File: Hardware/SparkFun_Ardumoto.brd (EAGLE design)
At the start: 59.7 x 53.3 mm, 64 parts, among them U1 ARDUINO, U2 L298, U5 74HC1G04, U6 74HC1G04

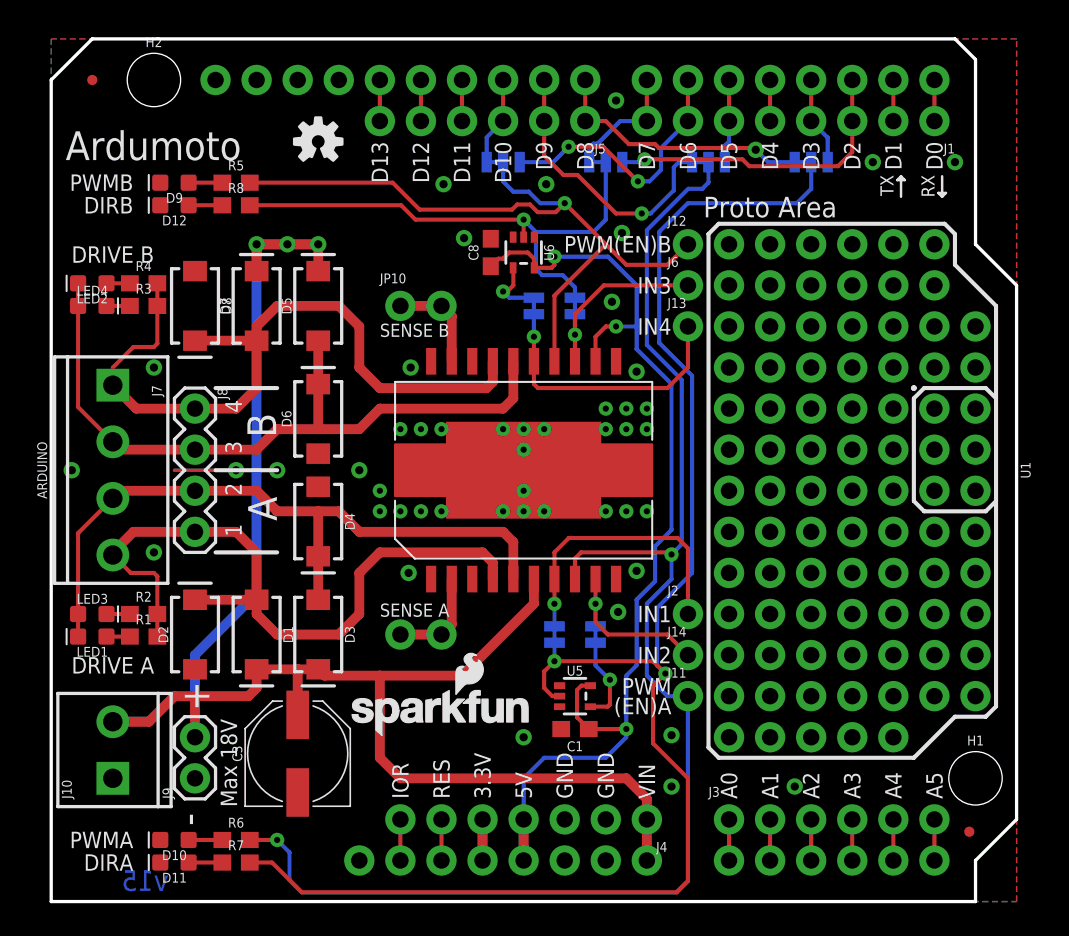
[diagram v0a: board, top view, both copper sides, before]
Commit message: Made changes to prototype in preparation for reds
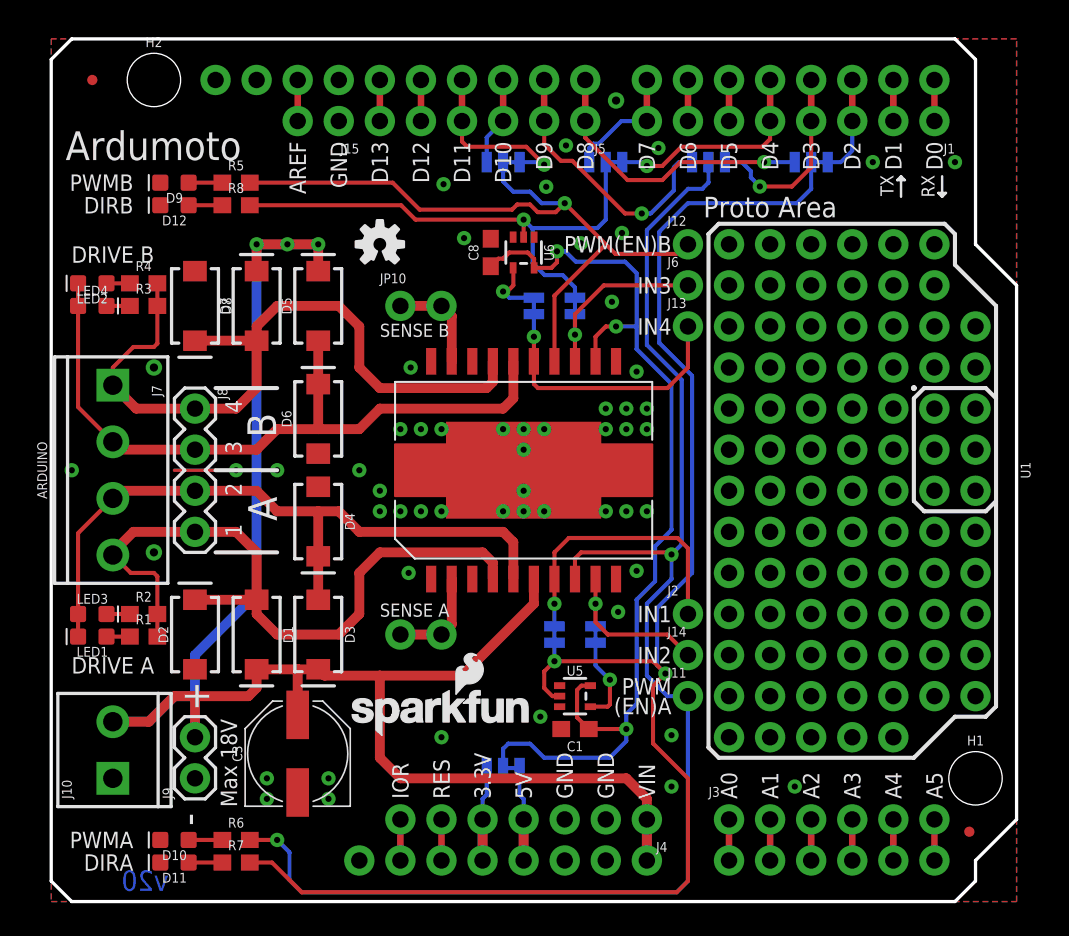
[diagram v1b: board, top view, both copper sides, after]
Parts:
- added J15: (no value), SparkFun-Connectors:1X02_NO_SILK
- added JP11: 31NCT, SparkFun-Jumpers:SMT-JUMPER_3_1-NC_TRACE_SILK
- moved U$1 7.41 mm to (20.3, 40.6)
- turned JP1 to 180 degrees
- turned JP2 to 180 degrees
- turned JP3 to 180 degrees
- turned JP4 to 180 degrees
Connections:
- new net N$10: J15.2, U1.AREF
- new net VCCIO: C1.1, C8.1, JP11.2, U2.12, U5.5, U6.5
- net 3.3V: now also JP11.1
- net 5V: now also JP11.3; no longer C1.1, C8.1, U2.12, U5.5, U6.5
- net D10: now also JP4.1; no longer JP4.3
- net D11: now also JP4.3
- net D2: now also JP1.3; no longer JP3.1
- net D3: now also JP2.3; no longer JP1.1
- net D4: now also JP3.3
- net D5: no longer JP2.1
- net D6: no longer JP4.1
- net D7: now also JP3.1; no longer JP3.3
- net D8: now also JP1.1; no longer JP1.3
- net D9: now also JP2.1; no longer JP2.3
- net GND: now also J15.1
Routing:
- net VCCIO: track 0.00 -> 62.5 mm, vias 0 -> 3
- net 5V: track 66.7 -> 8.36 mm, vias 3 -> 0
- net D6: track 16.6 -> 2.54 mm, vias 2 -> 0
- net D2: track 19.3 -> 6.19 mm, vias 1 -> 0
- net D4: track 2.54 -> 14.6 mm, vias 0 -> 1
- net D11: track 2.54 -> 11.1 mm, vias 0 -> 1
- net D3: track 5.50 -> 12.1 mm, vias 0 -> 1
- net 3.3V: track 5.08 -> 8.36 mm
- net D5: track 5.19 -> 2.54 mm
- net N$10: track 0.00 -> 2.54 mm
- net D8: track 16.5 -> 18.1 mm
- net PWMB: track 44.6 -> 44.0 mm
- net GND: vias 48 -> 56
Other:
- outline, holes or cut-outs redrawn
- board text added: "AREF"
- board text added: "VCCIO"
- board text added: "v20"
- board text removed: "5"
- board text removed: "6"
- board text removed: "v15"

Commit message: Added note on VCCIO and nudged traces
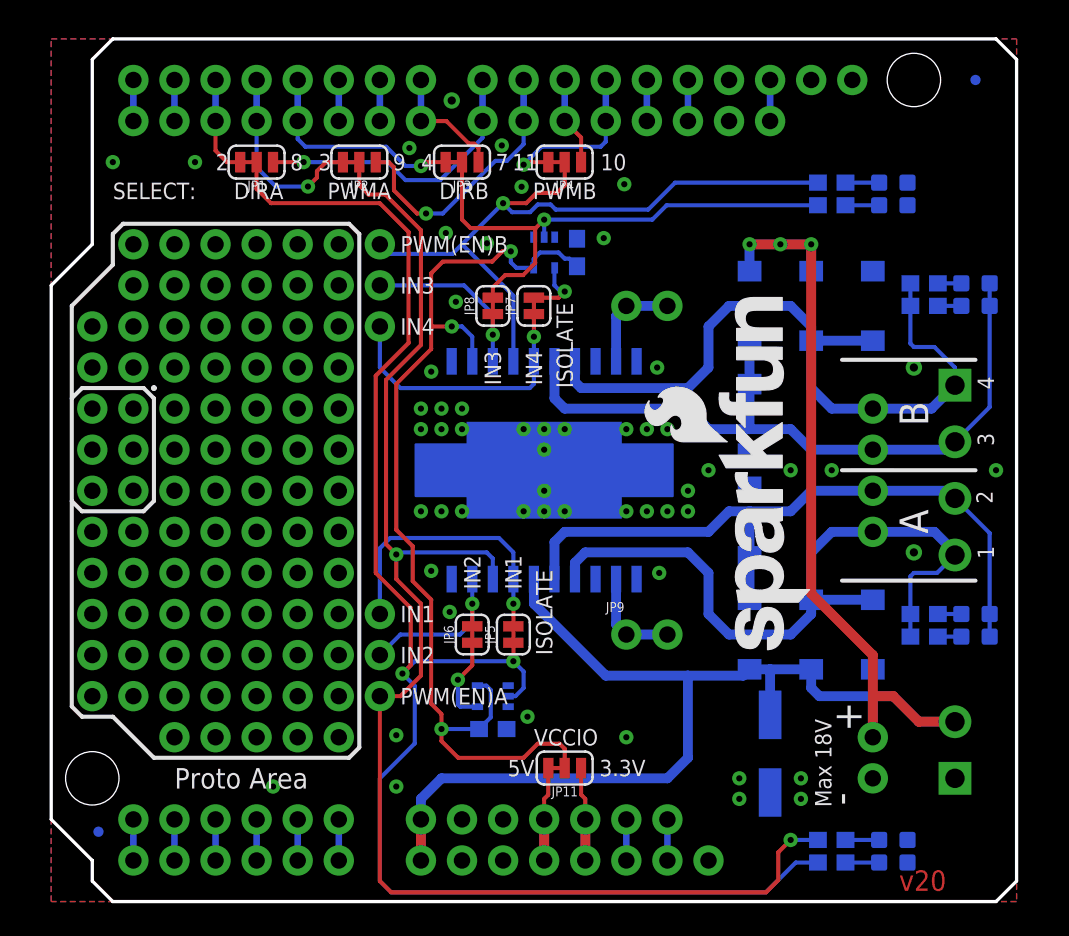
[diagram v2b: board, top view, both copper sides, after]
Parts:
- moved FRAME2 105.4 mm to (82.5, -11.4), flipped to the bottom
- moved FRAME1 64.8 mm to (62.3, -15.2), flipped to the bottom
- moved FD1 54.6 mm to (57.1, 50.8), flipped to the bottom
- moved H1 54.6 mm to (2.54, 7.62), flipped to the bottom
- moved LED1 54.6 mm to (57.1, 16.4), flipped to the bottom
- moved LED2 54.6 mm to (57.1, 38.2), flipped to the bottom
- moved LED3 54.6 mm to (57.1, 17.8), flipped to the bottom
- moved LED4 54.6 mm to (57.1, 36.8), flipped to the bottom
- moved FD2 53.8 mm to (2.92, 4.32), flipped to the bottom
- moved J10 52.1 mm to (55.9, 7.62), flipped to the bottom
- moved J7 52.1 mm to (55.9, 31.9), flipped to the bottom
- moved J1 49.5 mm to (5.08, 48.3), flipped to the bottom
- moved R1 48.3 mm to (54.0, 16.4), flipped to the bottom
- moved R2 48.3 mm to (54.0, 17.8), flipped to the bottom
- moved R3 48.3 mm to (54.0, 36.8), flipped to the bottom
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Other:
- outline, holes or cut-outs redrawn

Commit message: Made post-review changes
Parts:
- moved FRAME2 105.4 mm to (-22.9, -11.4), flipped to the top
- moved FRAME1 64.8 mm to (-2.56, -15.2), flipped to the top
- moved FD1 54.6 mm to (2.54, 50.8), flipped to the top
- moved H1 54.6 mm to (57.1, 7.62), flipped to the top
- moved LED1 54.6 mm to (2.54, 16.4), flipped to the top
- moved LED2 54.6 mm to (2.54, 38.2), flipped to the top
- moved LED3 54.6 mm to (2.54, 17.8), flipped to the top
- moved LED4 54.6 mm to (2.54, 36.8), flipped to the top
- moved FD2 53.8 mm to (56.8, 4.32), flipped to the top
- moved J10 52.1 mm to (3.81, 7.62), flipped to the top
- moved J7 52.1 mm to (3.81, 31.9), flipped to the top
- moved J1 49.5 mm to (54.6, 48.3), flipped to the top
- moved R1 48.3 mm to (5.71, 16.4), flipped to the top
- moved R2 48.3 mm to (5.71, 17.8), flipped to the top
- moved R3 48.3 mm to (5.71, 36.8), flipped to the top
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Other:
- outline, holes or cut-outs redrawn

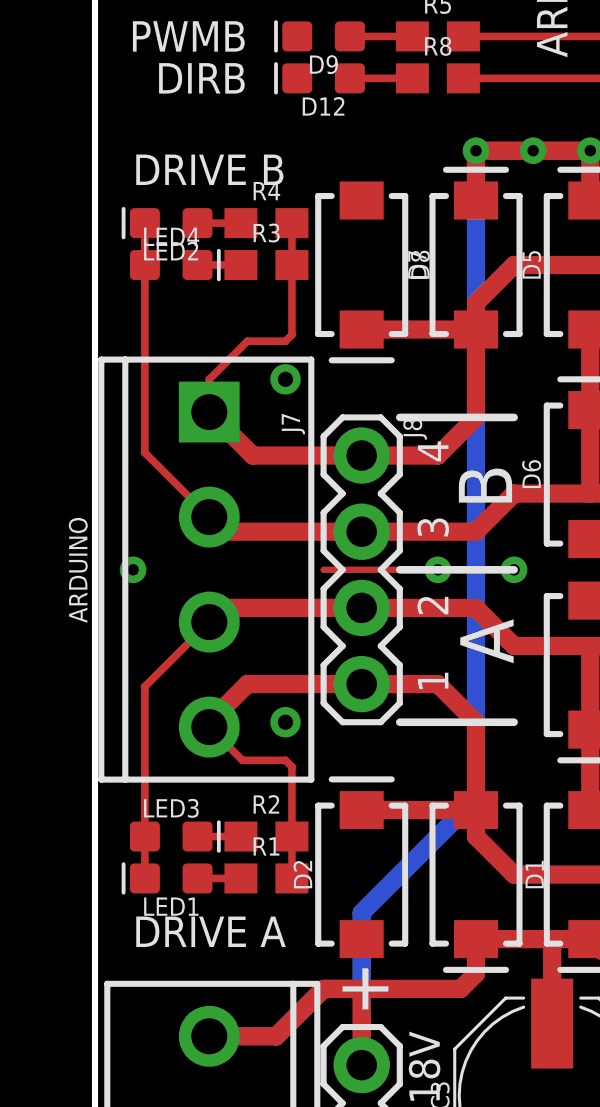
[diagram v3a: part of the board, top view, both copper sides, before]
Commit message: switched components LED1 and LED3
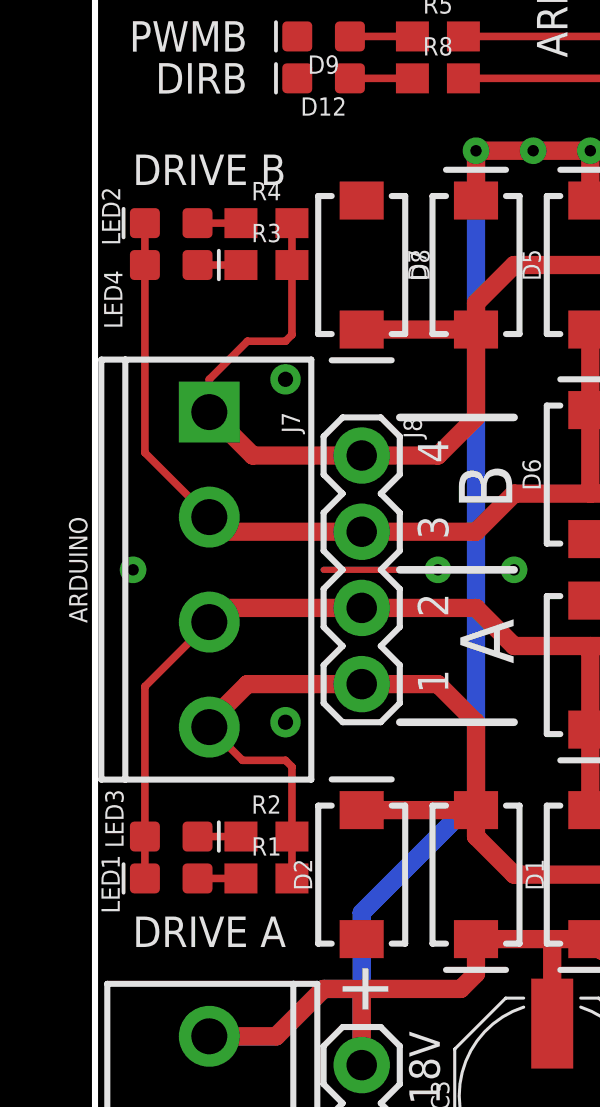
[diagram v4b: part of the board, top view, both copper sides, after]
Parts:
- LED1: value Yellow -> BLUE
- LED3: value BLUE -> Yellow
